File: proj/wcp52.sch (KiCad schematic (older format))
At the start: 8 parts, among them J2 IN1, J3 IN2, J4 OUT, J5 CONN-PJ-037A

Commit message: Layout most analog bits
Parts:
- removed J2: IN1, manuf:CONN-BNC-1-1337543-0, symbol CONN-BNC-1-1337543-0
- removed J3: IN2, manuf:CONN-BNC-1-1337543-0, symbol CONN-BNC-1-1337543-0
- removed J4: OUT, manuf:CONN-BNC-1-1337543-0, symbol CONN-BNC-1-1337543-0
- added J2: IN1, manuf:CONN-TE-1814400, symbol CONN-SMA-5-1814400-1
- added J3: IN2, manuf:CONN-TE-1814400, symbol CONN-SMA-5-1814400-1
- added J4: OUT, manuf:CONN-TE-1814400, symbol CONN-SMA-5-1814400-1
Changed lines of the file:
@@
 Wire Wire Line
 	1900 7550 1900 7500
-$Comp
-L CONN-BNC-1-1337543-0 J2
-U 1 1 54F6DB05
-P 12800 2300
-F 0 "J2" H 12800 2500 50  0000 C CNN
-F 1 "IN1" H 12800 2400 50  0000 C CNN
-F 2 "manuf:CONN-BNC-1-1337543-0" H 12800 2300 50  0001 C CNN
-F 3 "" H 12800 2300 50  0000 C CNN
-	1    12800 2300
-	-1   0    0    -1
-$EndComp
 Wire Wire Line
 	12700 2300 11700 2300
@@
 Wire Wire Line
 	12800 2450 12800 2400
-$Comp
-L CONN-BNC-1-1337543-0 J3
-U 1 1 54F6DFD5
-P 12800 2800
-F 0 "J3" H 12800 3000 50  0000 C CNN
-F 1 "IN2" H 12800 2900 50  0000 C CNN
-F 2 "manuf:CONN-BNC-1-1337543-0" H 12800 2800 50  0001 C CNN
-F 3 "" H 12800 2800 50  0000 C CNN
-	1    12800 2800
-	-1   0    0    -1
-$EndComp
 Wire Wire Line
 	12700 2800 12400 2800
@@
 Wire Wire Line
 	12800 2900 12800 2950
-$Comp
-L CONN-BNC-1-1337543-0 J4
-U 1 1 54F6E521
-P 12800 4200
-F 0 "J4" H 12800 4400 50  0000 C CNN
-F 1 "OUT" H 12800 4300 50  0000 C CNN
-F 2 "manuf:CONN-BNC-1-1337543-0" H 12800 4200 50  0001 C CNN
-F 3 "" H 12800 4200 50  0000 C CNN
-	1    12800 4200
-	-1   0    0    -1
-$EndComp
 Wire Wire Line
 	12700 4200 11700 4200
@@
 Wire Wire Line
 	1200 1950 1200 1900
+$Comp
+L CONN-SMA-5-1814400-1 J2
+U 1 1 54F77034
+P 12800 2300
+F 0 "J2" H 12800 2500 50  0000 C CNN
+F 1 "IN1" H 12800 2400 50  0000 C CNN
+F 2 "manuf:CONN-TE-1814400" H 12800 2300 50  0001 C CNN
+F 3 "" H 12800 2300 50  0000 C CNN
+F 4 "DIST DIGIKEY A97593-ND" H 12800 2300 60  0001 C CNN "BOM"
+	1    12800 2300
+	-1   0    0    -1
+$EndComp
+$Comp
+L CONN-SMA-5-1814400-1 J3
+U 1 1 54F77555
+P 12800 2800
+F 0 "J3" H 12800 3000 50  0000 C CNN
+F 1 "IN2" H 12800 2900 50  0000 C CNN
+F 2 "manuf:CONN-TE-1814400" H 12800 2800 50  0001 C CNN
+F 3 "" H 12800 2800 50  0000 C CNN
+F 4 "DIST DIGIKEY A97593-ND" H 12800 2800 60  0001 C CNN "BOM"
+	1    12800 2800
+	-1   0    0    -1
+$EndComp
+$Comp
+L CONN-SMA-5-1814400-1 J4
+U 1 1 54F777EC
+P 12800 4200
+F 0 "J4" H 12800 4400 50  0000 C CNN
+F 1 "OUT" H 12800 4300 50  0000 C CNN
+F 2 "manuf:CONN-TE-1814400" H 12800 4200 50  0001 C CNN
+F 3 "" H 12800 4200 50  0000 C CNN
+F 4 "DIST DIGIKEY A97593-ND" H 12800 4200 60  0001 C CNN "BOM"
+	1    12800 4200
+	-1   0    0    -1
+$EndComp
 $EndSCHEMATC

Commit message: Lots of layout work
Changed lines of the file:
@@
 F0 "MPU" 60
 F1 "MPU.sch" 60
+F2 "USBD_N" B L 5400 5500 50
+F3 "USBD_P" B L 5400 5600 50
+F4 "SER_TO_MPU" I L 5400 4500 50
+F5 "SER_FROM_MPU" O L 5400 4600 50
 $EndSheet
 $Sheet
@@
 F6 "#SLEEP" O R 3200 4200 50
 F7 "USBPWR" O R 3200 4100 50
+F8 "USBD_N" B R 3200 5500 50
+F9 "USBD_P" B R 3200 5600 50
 $EndSheet
 $Sheet
@@
 	-1   0    0    -1
 $EndComp
+Wire Wire Line
+	3200 5500 5400 5500
+Wire Wire Line
+	5400 5600 3200 5600
+Wire Wire Line
+	5400 4500 3200 4500
+Wire Wire Line
+	3200 4600 5400 4600
 $EndSCHEMATC

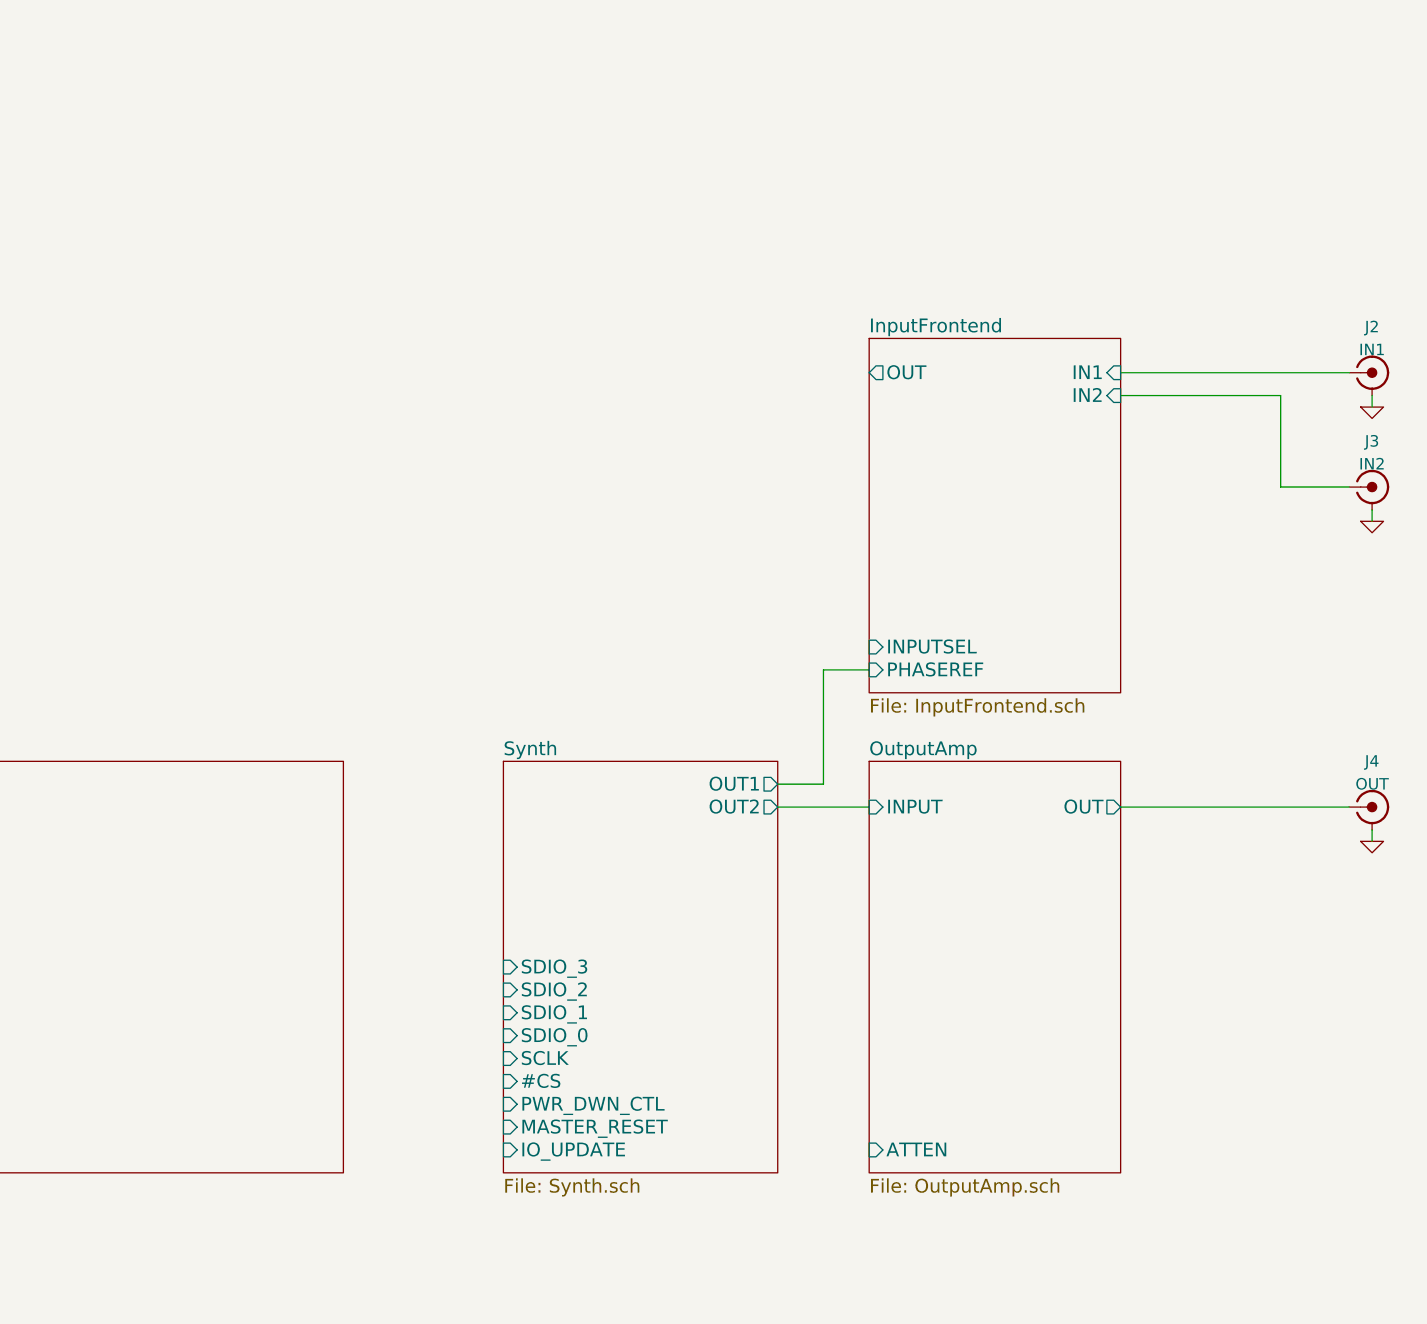
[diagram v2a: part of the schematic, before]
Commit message: All parts placed
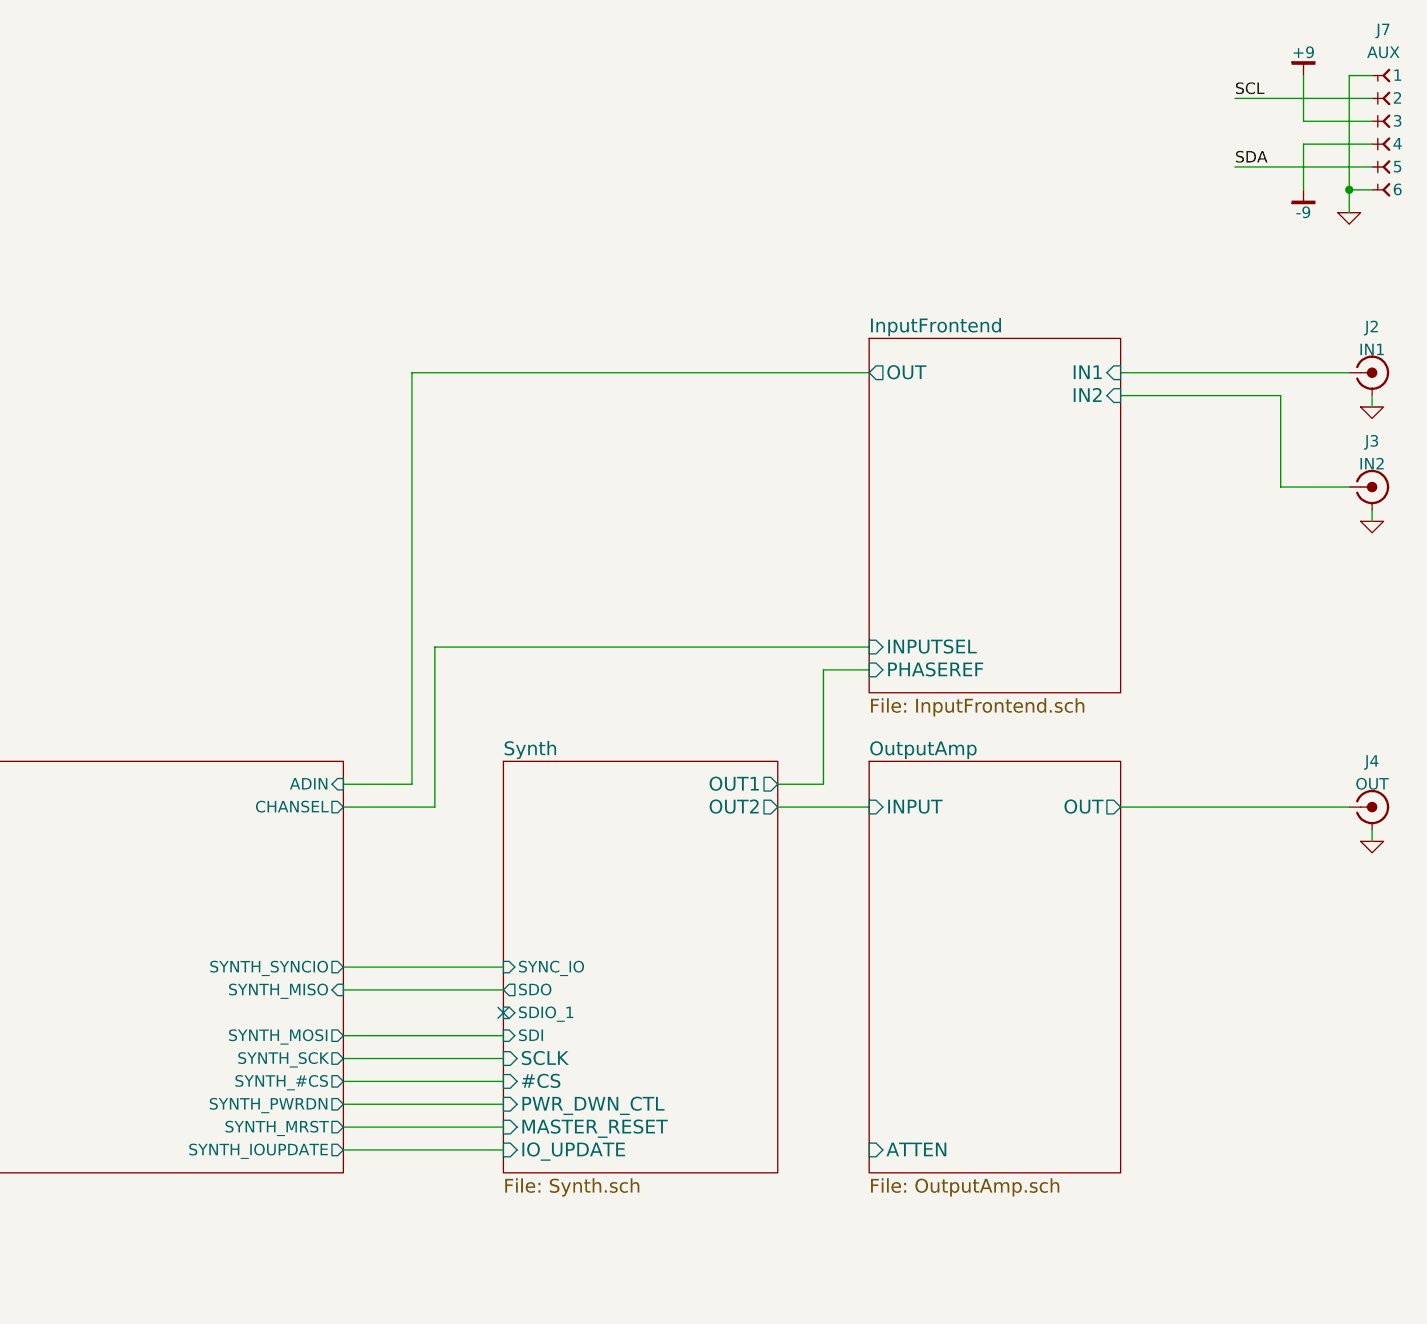
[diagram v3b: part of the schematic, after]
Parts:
- added J7: AUX, conn-100mil:CONN-100MIL-F-1x6, symbol CONN-100MIL-F-1x6
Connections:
- net +9: now also J7.3
- net -9: now also J7.4
- net GND: now also J7.1, J7.6
- new net SCL: J7.2
- new net SDA: J7.5
- no-connect marks 0 -> 1
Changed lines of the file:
@@
 F4 "SER_TO_MPU" I L 5400 4500 50
 F5 "SER_FROM_MPU" O L 5400 4600 50
+F6 "SYNTH_#CS" O R 8300 5400 50
+F7 "SYNTH_IOUPDATE" O R 8300 5700 50
+F8 "SYNTH_PWRDN" O R 8300 5500 50
+F9 "SYNTH_MRST" O R 8300 5600 50
+F10 "SYNTH_SYNCIO" O R 8300 4900 50
+F11 "CHANSEL" O R 8300 4200 50
+F12 "SYNTH_SCK" O R 8300 5300 50
+F13 "SYNTH_MISO" I R 8300 5000 50
+F14 "SYNTH_MOSI" O R 8300 5200 50
+F15 "ADIN" I R 8300 4100 50
 $EndSheet
 $Sheet
@@
 F5 "#CS" I L 9000 5400 60
 F6 "SCLK" I L 9000 5300 60
-F7 "SDIO_0" I L 9000 5200 60
-F8 "SDIO_1" I L 9000 5100 60
-F9 "SDIO_2" I L 9000 5000 60
-F10 "SDIO_3" I L 9000 4900 60
-F11 "OUT1" O R 10200 4100 60
-F12 "OUT2" O R 10200 4200 60
+F7 "OUT1" O R 10200 4100 60
+F8 "OUT2" O R 10200 4200 60
+F9 "SDI" I L 9000 5200 50
+F10 "SDIO_1" I L 9000 5100 50
+F11 "SDO" O L 9000 5000 50
+F12 "SYNC_IO" I L 9000 4900 50
 $EndSheet
 $Sheet
@@
 Wire Wire Line
 	3200 4600 5400 4600
+Wire Wire Line
+	8300 4900 9000 4900
+Wire Wire Line
+	8300 5000 9000 5000
+Wire Wire Line
+	8300 5200 9000 5200
+Wire Wire Line
+	8300 5300 9000 5300
+Wire Wire Line
+	8300 5400 9000 5400
+Wire Wire Line
+	8300 5500 9000 5500
+Wire Wire Line
+	8300 5600 9000 5600
+Wire Wire Line
+	8300 5700 9000 5700
+NoConn ~ 9000 5100
+Wire Wire Line
+	8300 4200 8700 4200
+Wire Wire Line
+	8700 4200 8700 3500
+Wire Wire Line
+	8700 3500 10600 3500
+Wire Wire Line
+	8300 4100 8600 4100
+Wire Wire Line
+	8600 4100 8600 2300
+Wire Wire Line
+	8600 2300 10600 2300
+$Comp
+L CONN-100MIL-F-1x6 J7
+U 1 1 54F9C82B
+P 12850 1000
+F 0 "J7" H 12850 1200 50  0000 C CNN
+F 1 "AUX" H 12850 1100 50  0000 C CNN
+F 2 "conn-100mil:CONN-100MIL-F-1x6" H 12850 1000 50  0001 C CNN
+F 3 "" H 12850 1000 50  0000 C CNN
+	1    12850 1000
+	1    0    0    -1
+$EndComp
+Wire Wire Line
+	12800 1000 12700 1000
+Wire Wire Line
+	12700 1000 12700 1600
+Wire Wire Line
+	12800 1500 12700 1500
+Connection ~ 12700 1500
+$Comp
+L GND #PWR016
+U 1 1 54F9CCD1
+P 12700 1600
+F 0 "#PWR016" H 12700 1600 30  0001 C CNN
+F 1 "GND" H 12700 1530 30  0001 C CNN
+F 2 "" H 12700 1600 60  0000 C CNN
+F 3 "" H 12700 1600 60  0000 C CNN
+	1    12700 1600
+	1    0    0    -1
+$EndComp
+Wire Wire Line
+	12800 1100 12200 1100
+Text Label 12200 1100 0    50   ~ 0
+SCL
+Text Label 12200 1400 0    50   ~ 0
+SDA
+Wire Wire Line
+	12200 1400 12800 1400
+Wire Wire Line
+	12800 1200 12500 1200
+Wire Wire Line
+	12500 1200 12500 1000
+$Comp
+L +9 #PWR017
+U 1 1 54F9D70F
+P 12500 1000
+F 0 "#PWR017" H 12500 1050 30  0001 C CNN
+F 1 "+9" H 12500 1100 50  0000 C CNN
+F 2 "" H 12500 1000 60  0000 C CNN
+F 3 "" H 12500 1000 60  0000 C CNN
+	1    12500 1000
+	1    0    0    -1
+$EndComp
+$Comp
+L -9 #PWR018
+U 1 1 54F9D873
+P 12500 1500
+F 0 "#PWR018" H 12500 1450 30  0001 C CNN
+F 1 "-9" H 12500 1400 50  0000 C CNN
+F 2 "" H 12500 1500 60  0000 C CNN
+F 3 "" H 12500 1500 60  0000 C CNN
+	1    12500 1500
+	1    0    0    -1
+$EndComp
+Wire Wire Line
+	12500 1500 12500 1300
+Wire Wire Line
+	12500 1300 12800 1300
 $EndSCHEMATC
